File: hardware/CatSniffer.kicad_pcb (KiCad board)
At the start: 4 copper layers, 81 x 20 mm, 100 parts, among them J1 Antenna, J3 Conn_01x06_Female, P1 USB_C_Plug_USB2.0, SW1 SW, U1 AP2112K-3.3, U2 RFSW8006QTR7, U3 RP2040, U4 0900PC15A0036, U5 0900FM15D0039, U6 PE42421, U7 SX1262IMLTRT, U8 CC1352P1F3RGZT, U9 W25Q16JV, Y1 48MHz, Y2 32.768kHz, Y3 32Mhz, Y4 12MHz

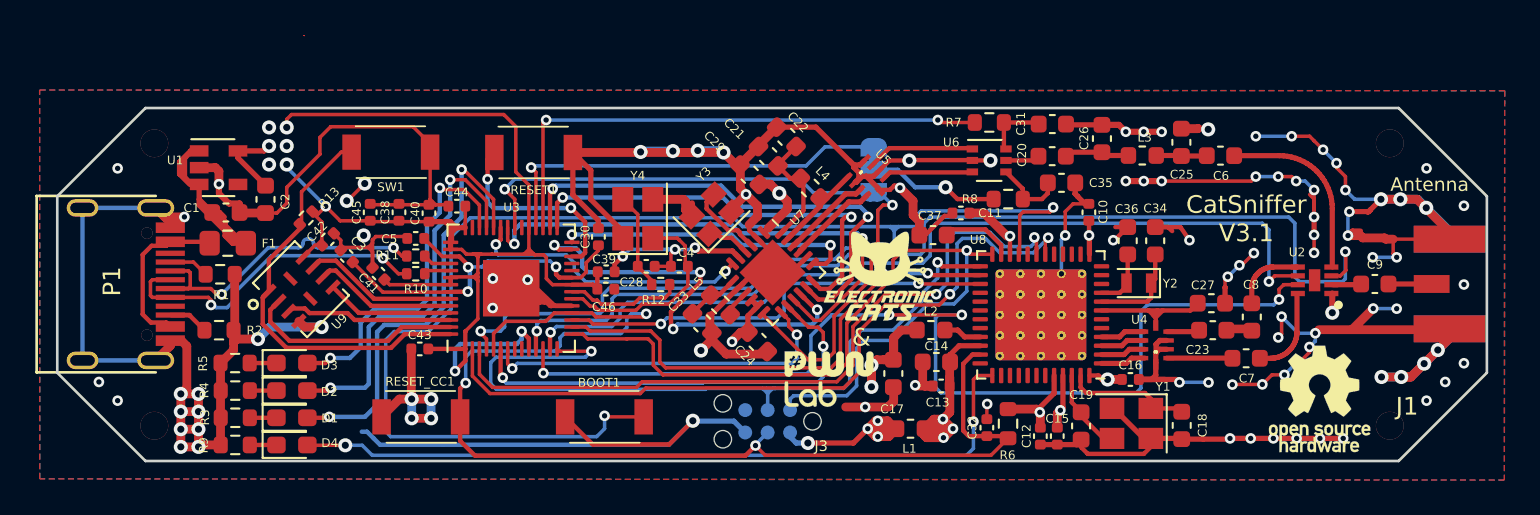
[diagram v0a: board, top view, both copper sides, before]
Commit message: Enlarged U4, U5 and update PCB
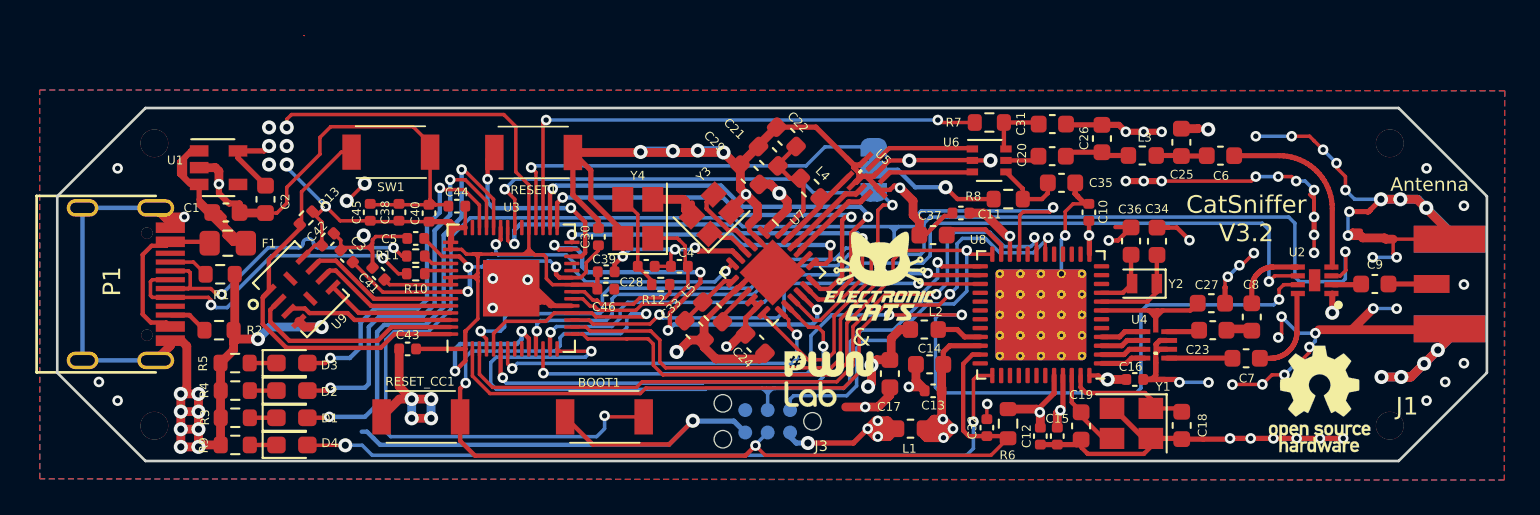
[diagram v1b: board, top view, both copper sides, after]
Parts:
- moved C43 0.69 mm to (104.8, 113.7)
- moved C33 0.59 mm to (121.1, 112.6)
- moved L5 0.59 mm to (122.1, 111.6)
- moved C13 0.53 mm to (134.6, 116.0)
- moved C14 0.41 mm to (134.4, 114.5)
- moved L2 0.38 mm to (134.1, 112.5)
- moved Y2 0.32 mm to (146.6, 110.0)
- moved C16 0.25 mm to (146.1, 115.4)
- moved C17 0.20 mm to (132.2, 115.0)
- moved C36 0.19 mm to (145.8, 107.5)
- moved C24 0.16 mm to (124.5, 113.3)
- moved C34 0.10 mm to (147.3, 107.5)
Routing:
- net /VDDR: track 30.8 -> 29.6 mm
- net /VDDS: track 58.4 -> 57.4 mm
- net GND: track 425.2 -> 425.9 mm
- net Net-(U7-VREG): track 3.02 -> 3.64 mm
- net Net-(U7-DCC_SW): track 1.52 -> 2.12 mm
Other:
- board text added: "CatSniffer V3.2"
- board text removed: "CatSniffer V3.1"

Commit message: feat(Hw): Update labels
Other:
- board text added: "CatSniffer v3.2"
- board text removed: "CatSniffer v3.1"
